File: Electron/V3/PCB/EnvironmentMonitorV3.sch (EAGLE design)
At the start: 16 parts, among them U1 HTU21DSMD, U2 BMP180, U4 LIGHTSENSORTEMT6000

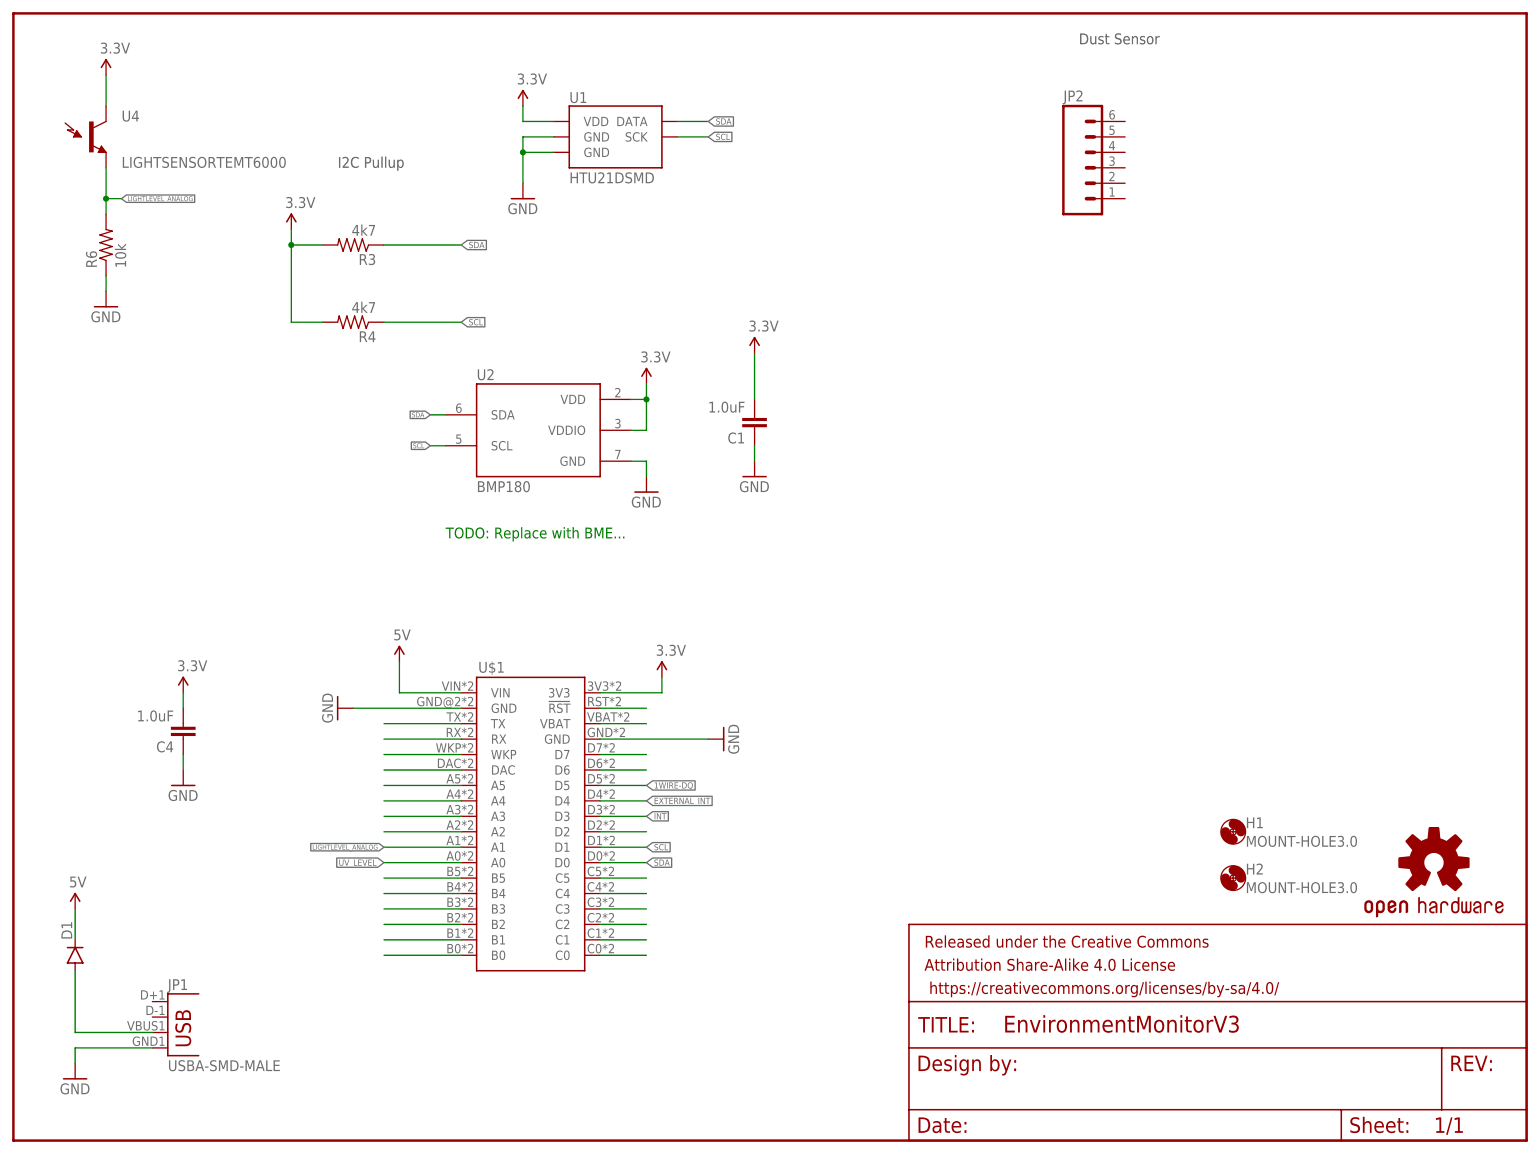
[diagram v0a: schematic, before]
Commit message: Added BME680 to V3 and removed other sensors (except light).
Added images for V2 and V3 PCBs.

PCBs sent to DirtyPCB for fab.
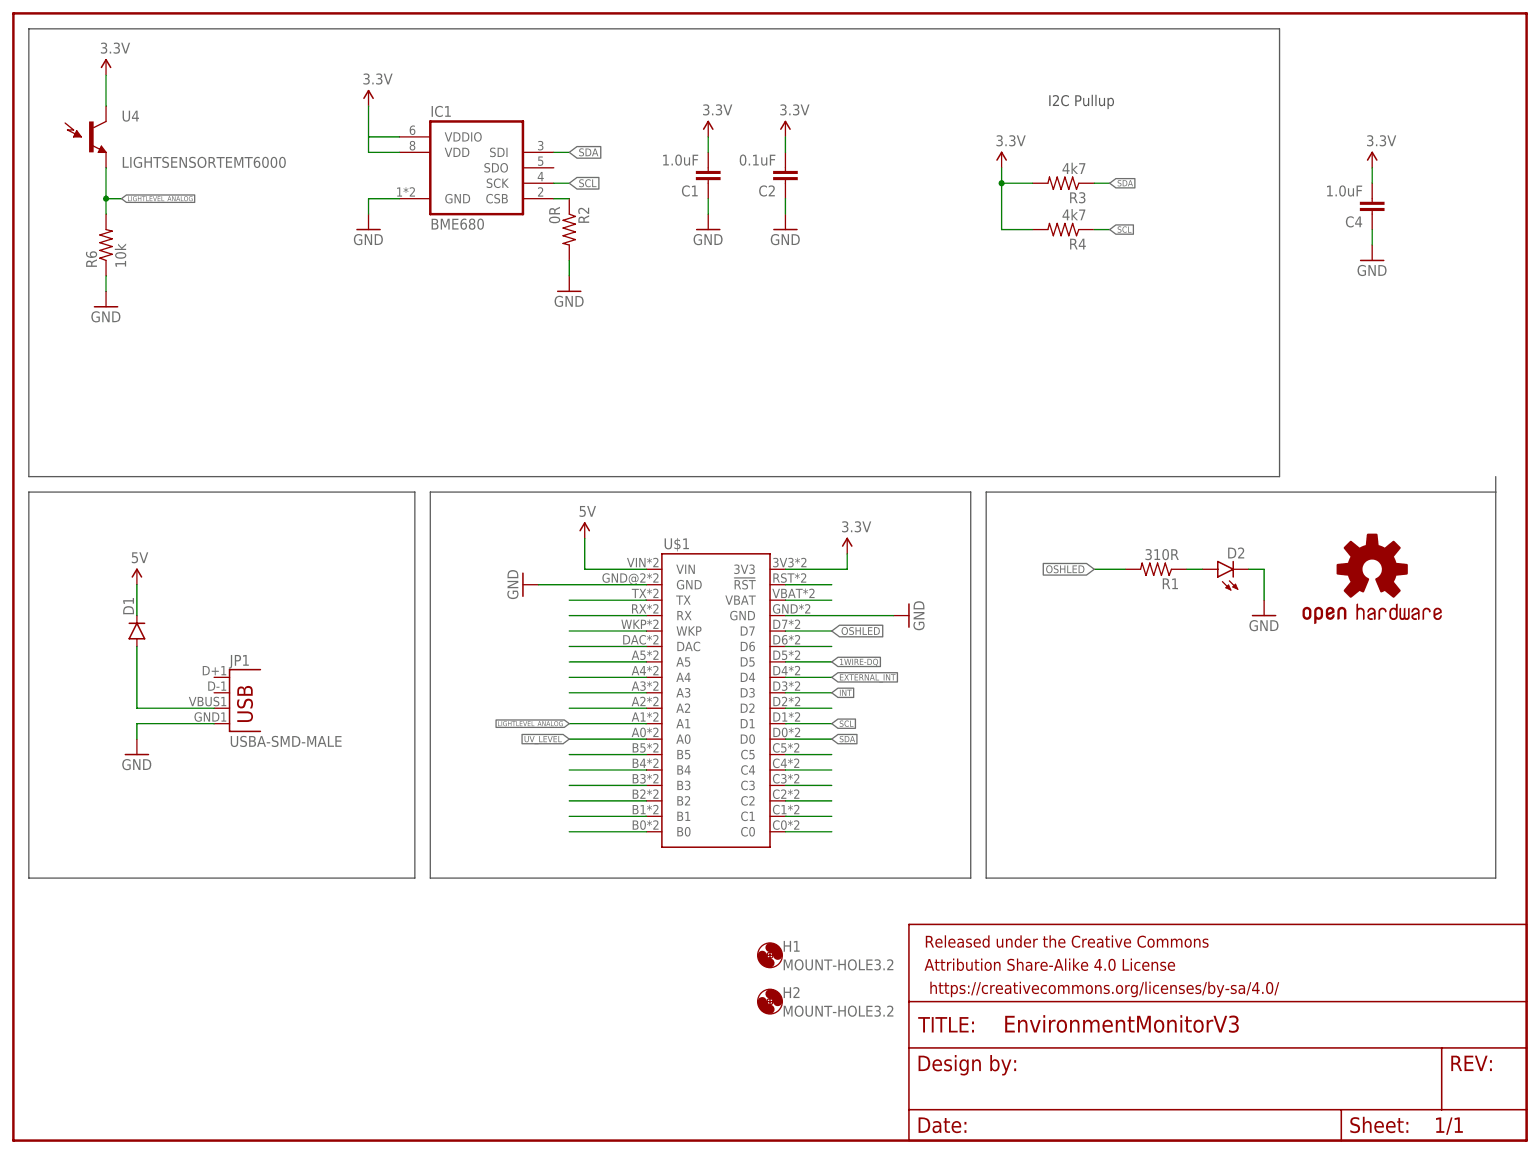
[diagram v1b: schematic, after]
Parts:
- removed JP2: (no value), SparkFun-Connectors:M06POLAR
- removed U1: HTU21DSMD, SparkFun-Sensors:HTU21DSMD
- removed U2: BMP180, SparkFun-Sensors:BMP180
- added C2: 0.1uF, SparkFun-Capacitors:1.0UF-25V-+80/-20(0805)"
- added D2: (no value), SparkFun-LED:LED1206-BOTTOM
- added IC1: BME680, bosch-bme680:BME680
- added R1: 310R, SparkFun-Resistors:RESISTOR0805-RES
- added R2: 0R, SparkFun-Resistors:RESISTOR0805-RES
- H1, H2: value MOUNT-HOLE3.0 -> MOUNT-HOLE3.2; device holes:MOUNT-HOLE3.0 -> holes:MOUNT-HOLE3.2
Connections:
- new net N$6: D2.A, R1.1
- new net OSHLED: R1.2, U$1.D7
- net 3.3V: now also C2.2, IC1.VDD, IC1.VDDIO; no longer U1.VDD, U2.VDD, U2.VDDIO
- net GND: now also C2.1, D2.C, IC1.GND, R2.2; no longer U1.GND@2, U1.GND@7, U2.GND
- net N$3: now also IC1.CSB, R2.1; no longer U$1.D7
- net SCL: now also IC1.SCK; no longer U1.SCK, U2.SCL
- net SDA: now also IC1.SDI; no longer U1.DATA, U2.SDA
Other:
- note removed: "Dust Sensor"
- note removed: "TODO: Replace with BME..."
- moved on the sheet: C1, C4, D1, H1, H2, JP1, R3, R4, U$1

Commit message: Minor tidyup
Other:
- note added: "Stephen Harrison"
- note added: "V3.0"
- moved on the sheet: C4, H1, H2
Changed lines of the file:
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@@
 <text x="170.18" y="170.18" size="1.778" layer="97">I2C Pullup</text>
 <wire x1="2.54" y1="182.88" x2="2.54" y2="109.22" width="0.1524" layer="97"/>
-<wire x1="2.54" y1="109.22" x2="208.28" y2="109.22" width="0.1524" layer="97"/>
-<wire x1="208.28" y1="109.22" x2="208.28" y2="182.88" width="0.1524" layer="97"/>
-<wire x1="208.28" y1="182.88" x2="2.54" y2="182.88" width="0.1524" layer="97"/>
+<wire x1="2.54" y1="109.22" x2="195.58" y2="109.22" width="0.1524" layer="97"/>
+<wire x1="195.58" y1="109.22" x2="195.58" y2="182.88" width="0.1524" layer="97"/>
+<wire x1="195.58" y1="182.88" x2="2.54" y2="182.88" width="0.1524" layer="97"/>
 <wire x1="68.58" y1="106.68" x2="157.48" y2="106.68" width="0.1524" layer="97"/>
 <wire x1="157.48" y1="106.68" x2="157.48" y2="43.18" width="0.1524" layer="97"/>
@@
 <wire x1="160.02" y1="43.18" x2="243.84" y2="43.18" width="0.1524" layer="97"/>
 <wire x1="243.84" y1="43.18" x2="243.84" y2="106.68" width="0.1524" layer="97"/>
-<wire x1="243.84" y1="109.22" x2="243.84" y2="106.68" width="0.1524" layer="97"/>
 <wire x1="243.84" y1="106.68" x2="160.02" y2="106.68" width="0.1524" layer="97"/>
+<wire x1="198.12" y1="182.88" x2="243.84" y2="182.88" width="0.1524" layer="97"/>
+<wire x1="243.84" y1="182.88" x2="243.84" y2="154.94" width="0.1524" layer="97"/>
+<wire x1="243.84" y1="154.94" x2="198.12" y2="154.94" width="0.1524" layer="97"/>
+<wire x1="198.12" y1="154.94" x2="198.12" y2="182.88" width="0.1524" layer="97"/>
+<text x="238.76" y="7.62" size="1.778" layer="97">V3.0</text>
+<text x="166.116" y="11.684" size="1.778" layer="97">Stephen Harrison</text>
 </plain>
 <instances>
@@
 <instance part="R4" gate="G$1" x="172.72" y="149.86" rot="R180"/>
 <instance part="SUPPLY10" gate="G$1" x="162.56" y="160.02"/>
-<instance part="C4" gate="G$1" x="223.52" y="154.94" rot="R180"/>
-<instance part="H1" gate="G$1" x="124.46" y="30.48"/>
-<instance part="H2" gate="G$1" x="124.46" y="22.86"/>
+<instance part="C4" gate="G$1" x="50.8" y="162.56" rot="R180"/>
+<instance part="H1" gate="G$1" x="205.74" y="175.26"/>
+<instance part="H2" gate="G$1" x="205.74" y="165.1"/>
 <instance part="LOGO1" gate="G$1" x="223.52" y="93.98"/>
-<instance part="SUPPLY14" gate="G$1" x="223.52" y="160.02"/>
-<instance part="GND13" gate="1" x="223.52" y="144.78"/>
+<instance part="SUPPLY14" gate="G$1" x="50.8" y="167.64"/>
+<instance part="GND13" gate="1" x="50.8" y="152.4"/>
 <instance part="U4" gate="G$1" x="12.7" y="165.1"/>
 <instance part="R6" gate="G$1" x="15.24" y="147.32" rot="R90"/>
@@
 <pinref part="C4" gate="G$1" pin="1"/>
 <pinref part="GND13" gate="1" pin="GND"/>
-<wire x1="223.52" y1="149.86" x2="223.52" y2="147.32" width="0.1524" layer="91"/>
+<wire x1="50.8" y1="157.48" x2="50.8" y2="154.94" width="0.1524" layer="91"/>
 </segment>
 <segment>
@@
 <pinref part="SUPPLY14" gate="G$1" pin="3.3V"/>
 <pinref part="C4" gate="G$1" pin="2"/>
-<wire x1="223.52" y1="160.02" x2="223.52" y2="157.48" width="0.1524" layer="91"/>
+<wire x1="50.8" y1="167.64" x2="50.8" y2="165.1" width="0.1524" layer="91"/>
 </segment>
 <segment>

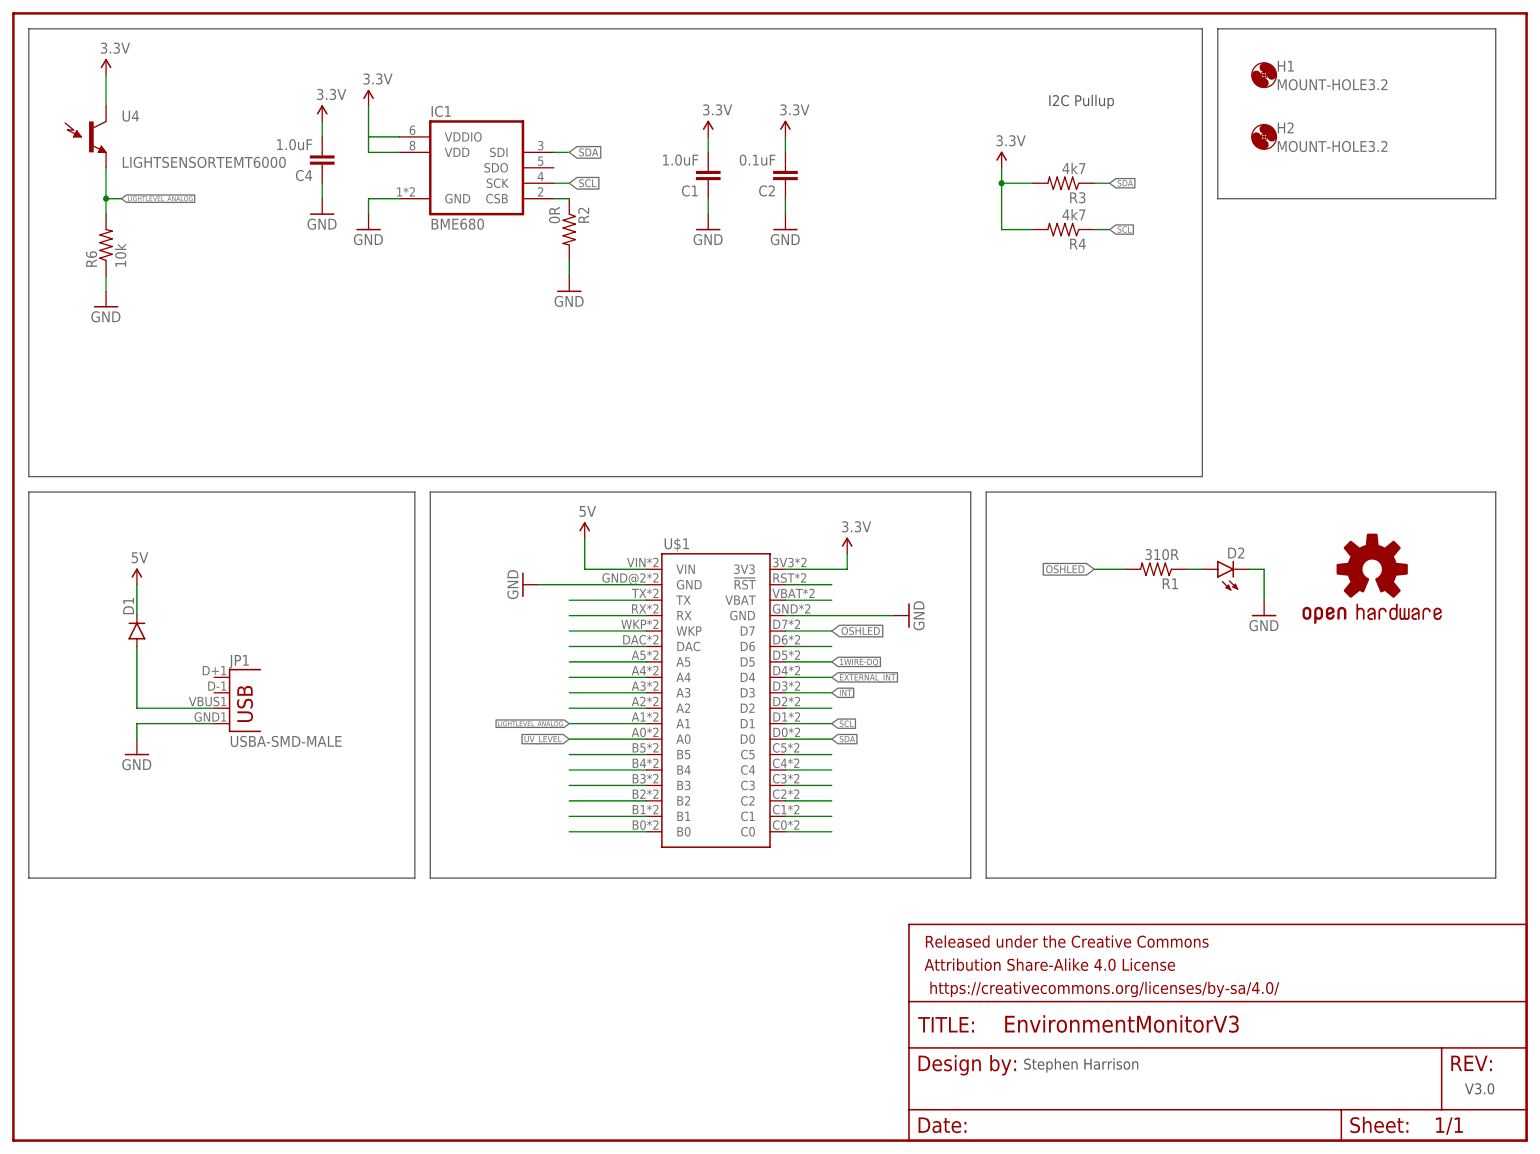
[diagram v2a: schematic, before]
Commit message: Updated with light sensor and BME680
*** DO NOT USE *** BME680 pads flipped.
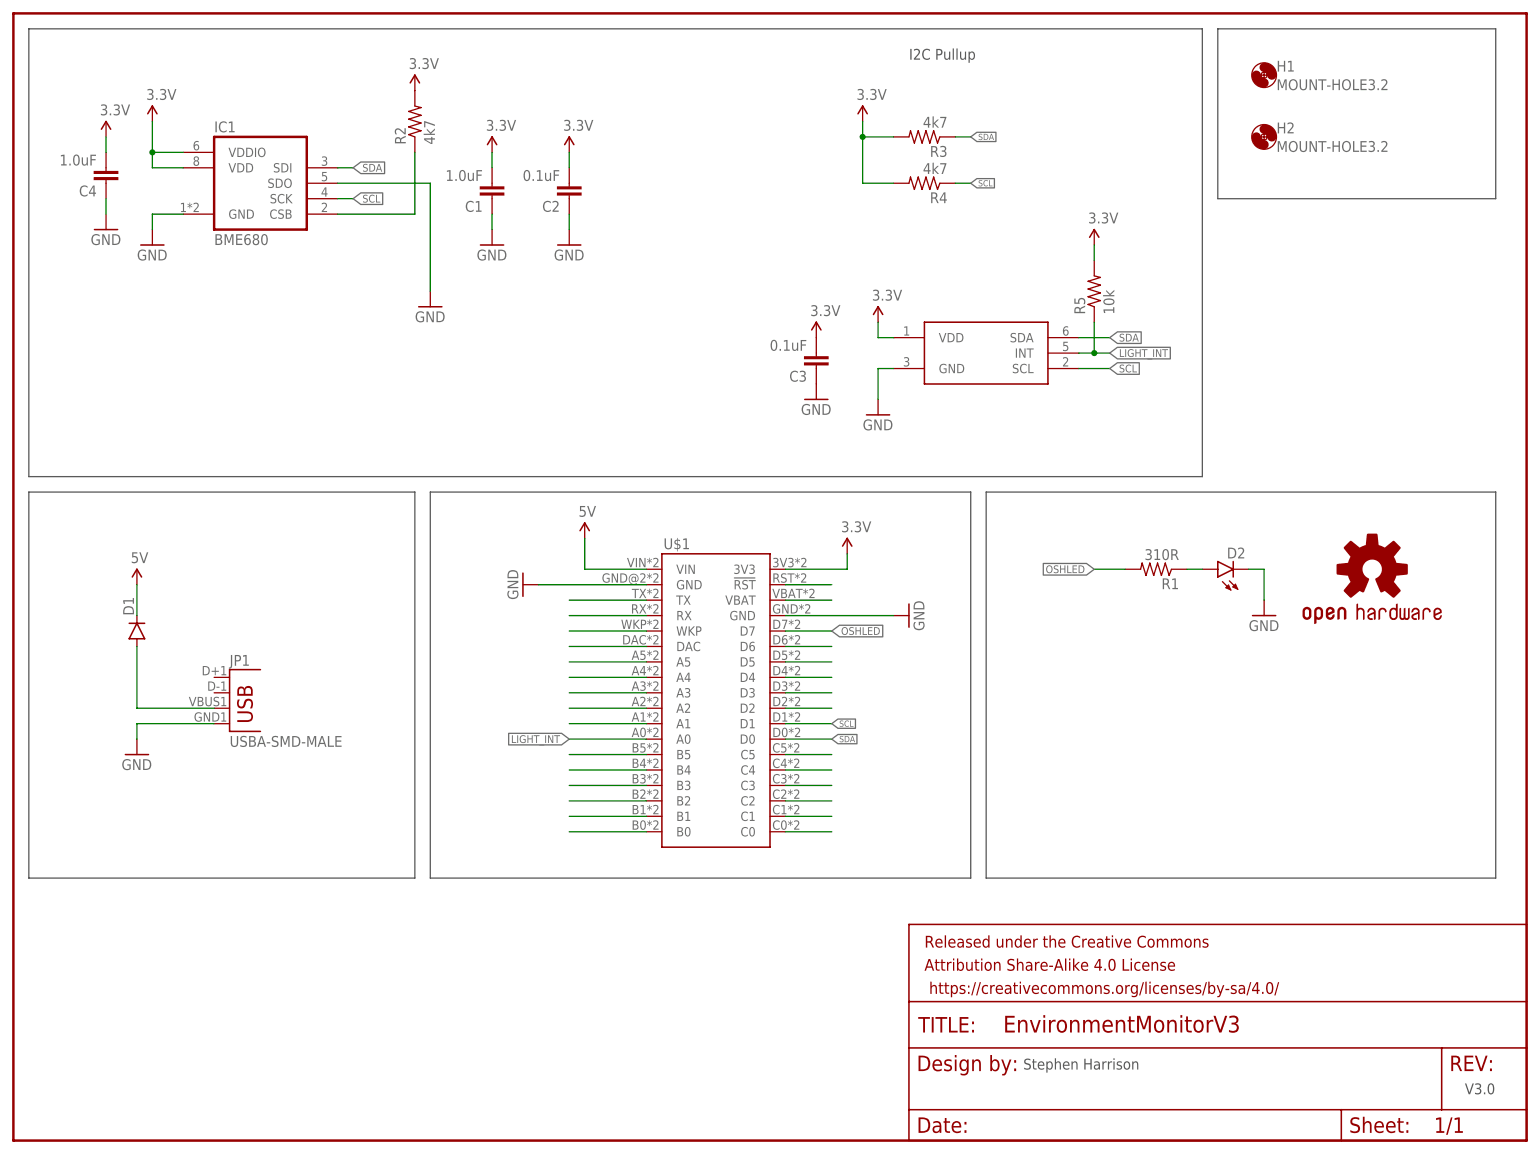
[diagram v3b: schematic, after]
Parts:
- removed R6: 10k, SparkFun-Resistors:RESISTOR0805-RES
- removed U4: LIGHTSENSORTEMT6000, SparkFun-Sensors:LIGHTSENSORTEMT6000
- added C3: 0.1uF, SparkFun-Capacitors:1.0UF-25V-+80/-20(0805)"
- added R5: 10k, SparkFun-Resistors:RESISTOR0805-RES
- added U$2: TCS3472, TCS3472:TCS3472
- R2: value 0R -> 4k7
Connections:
- net 1WIRE-DQ renamed N$7
- net EXTERNAL_INT renamed N$9
- net INT renamed N$10
- removed net LIGHTLEVEL_ANALOG: R6.2, U$1.A1, U4.E1
- removed net UV_LEVEL: U$1.A0
- new net LIGHT_INT: R5.1, U$1.A0, U$2.INT
- new net N$23: U$1.A1
- net 3.3V: now also C3.2, R2.2, R5.2, U$2.VDD; no longer U4.C1
- net GND: now also C3.1, IC1.SDO, U$2.GND; no longer R2.2, R6.1
- net SCL: now also U$2.SCL
- net SDA: now also U$2.SDA
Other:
- moved on the sheet: C1, C2, C4, IC1, R2, R3, R4
